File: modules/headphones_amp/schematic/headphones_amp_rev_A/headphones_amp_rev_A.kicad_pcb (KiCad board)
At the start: 2 copper layers, 24 parts, among them Q1 BC140, Q2 BC160, Q3 BC548, Q4 BC557, Q5 BC548, Q6 BC548

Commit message: added new references to the PPL
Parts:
- added C3: 220µ, Capacitor_THT:CP_Radial_D10.0mm_P5.00mm, F.Cu at (125.4, 64.0)
- added Q7: BC548, Package_TO_SOT_THT:TO-92L_Inline_Wide, F.Cu at (112.0, 111.4)
- added R13: 3.3k, Resistor_THT:R_Axial_DIN0207_L6.3mm_D2.5mm_P10.16mm_Horizontal, F.Cu at (110.2, 47.4)
- added R14: 1.5k, Resistor_THT:R_Axial_DIN0207_L6.3mm_D2.5mm_P10.16mm_Horizontal, F.Cu at (110.2, 51.5)
- added R15: 820, Resistor_THT:R_Axial_DIN0207_L6.3mm_D2.5mm_P10.16mm_Horizontal, F.Cu at (110.2, 55.5)
- added R16: 15k, Resistor_THT:R_Axial_DIN0207_L6.3mm_D2.5mm_P10.16mm_Horizontal, F.Cu at (110.2, 59.6)
- added R17: 56k, Resistor_THT:R_Axial_DIN0207_L6.3mm_D2.5mm_P10.16mm_Horizontal, F.Cu at (110.2, 63.6)
- added R18: 33k, Resistor_THT:R_Axial_DIN0207_L6.3mm_D2.5mm_P10.16mm_Horizontal, F.Cu at (110.2, 67.7)
- added R19: 10k, Resistor_THT:R_Axial_DIN0207_L6.3mm_D2.5mm_P10.16mm_Horizontal, F.Cu at (110.2, 71.7)
- added RV1: 820, Potentiometer_THT:Potentiometer_Bourns_3296W_Vertical, F.Cu at (130.0, 48.6)
- added RV2: 2.2k, Potentiometer_THT:Potentiometer_Bourns_3296W_Vertical, F.Cu at (130.0, 55.0)
- added TP1: TestPoint, TestPoint:TestPoint_Pad_D2.0mm, F.Cu at (135.0, 47.4)
- added TP2: TestPoint, TestPoint:TestPoint_Pad_D2.0mm, F.Cu at (135.0, 51.5)
- C1: value 100µ -> 220µ
- R5: value 1.2k -> 2.2k
- R8: value 330 -> 470
- moved R2 67.2 mm to (128.6, 117.5), turned to 180 degrees
- moved C1 59.7 mm to (137.0, 114.0)
- moved R1 56.6 mm to (118.4, 110.0)
- moved Q1 36.2 mm to (118.5, 104.5), turned to 90 degrees
- moved Q2 35.8 mm to (118.5, 124.5), turned to -90 degrees
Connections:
- C1 pad 2: unconnected-(C1-Pad2) -> Net-(C1-Pad2)
- Q1 pad 2: Net-(D1-A) -> Net-(Q1-B)
- Q2 pad 2: Net-(D3-K) -> Net-(Q2-B)
- Q5 pad 1: Net-(D3-K) -> Net-(Q2-B)
- Q5 pad 2: unconnected-(Q5-B-Pad2) -> Net-(Q5-B)
- R5 pad 2: Net-(D1-A) -> Net-(Q1-B)

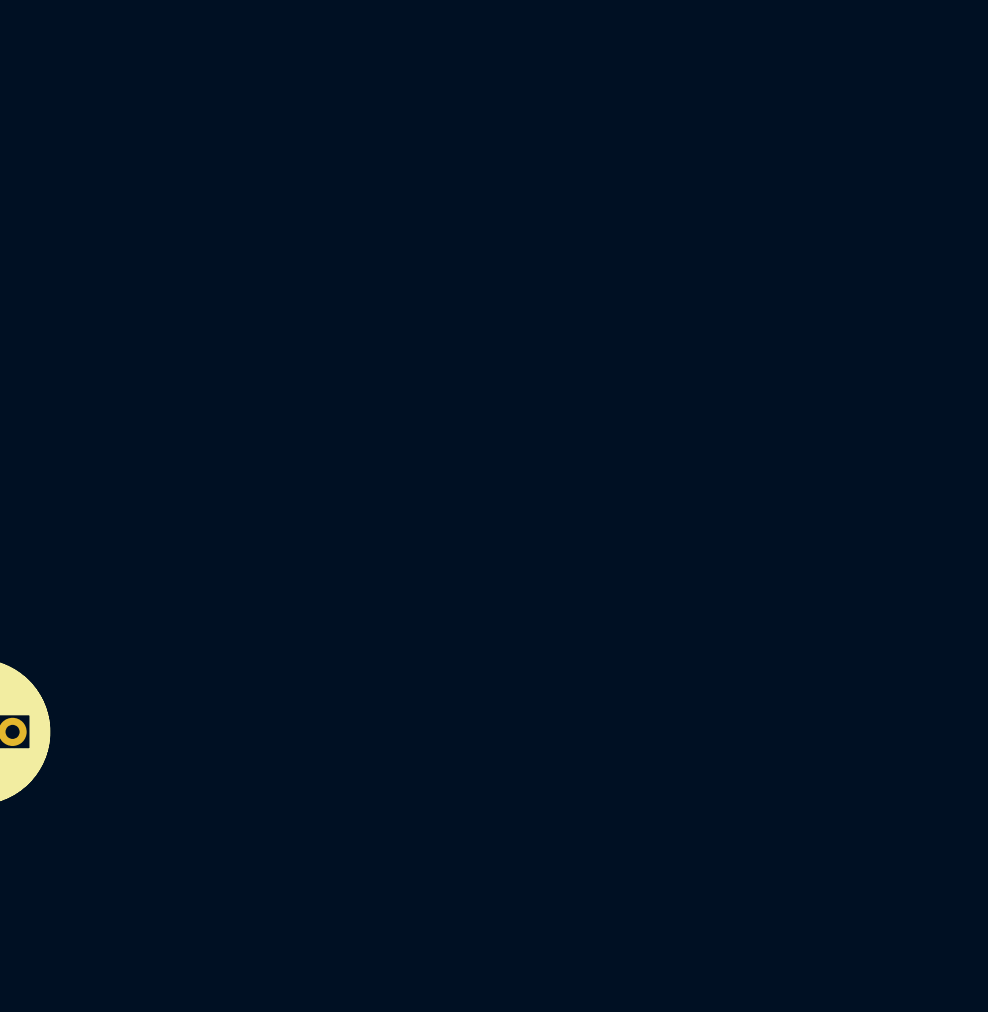
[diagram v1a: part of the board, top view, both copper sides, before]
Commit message: added proper silkscreen on PTV potentiometer
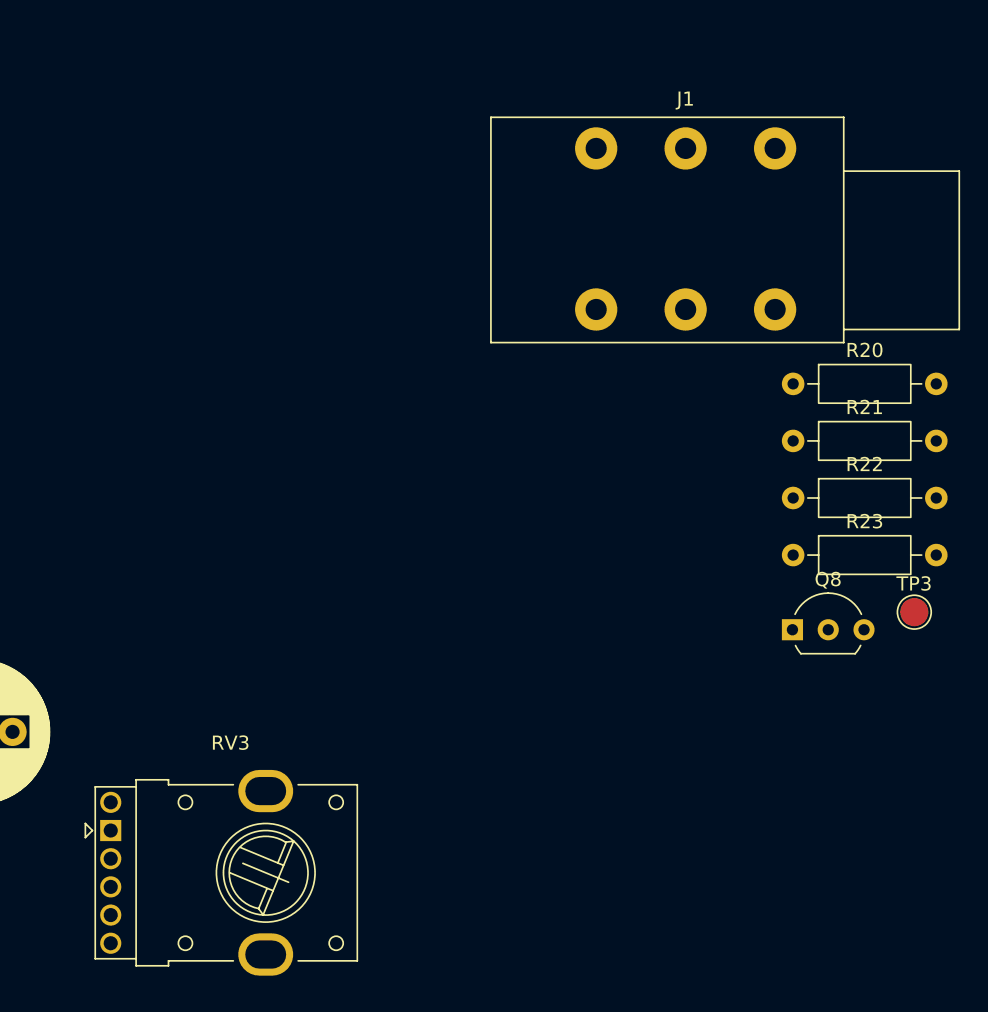
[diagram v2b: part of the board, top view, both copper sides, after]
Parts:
- added J1: AudioJack3_SwitchTR, Connector_Audio:Jack_6.35mm_Neutrik_NRJ6HM-1-PRE_Horizontal, F.Cu at (183.4, 72.6)
- added Q8: BC557, Package_TO_SOT_THT:TO-92L_Inline_Wide, F.Cu at (197.3, 106.8)
- added R20: 470, Resistor_THT:R_Axial_DIN0207_L6.3mm_D2.5mm_P10.16mm_Horizontal, F.Cu at (197.4, 89.3)
- added R21: 100, Resistor_THT:R_Axial_DIN0207_L6.3mm_D2.5mm_P10.16mm_Horizontal, F.Cu at (197.4, 93.3)
- added R22: 470, Resistor_THT:R_Axial_DIN0207_L6.3mm_D2.5mm_P10.16mm_Horizontal, F.Cu at (197.4, 97.4)
- added R23: 470, Resistor_THT:R_Axial_DIN0207_L6.3mm_D2.5mm_P10.16mm_Horizontal, F.Cu at (197.4, 101.5)
- added RV3: 68k, Potentiometer_THT:Potentiometer_Bourns_PTV112-4_Dual_Vertical, F.Cu at (149.0, 121.0)
- added TP3: TestPoint, TestPoint:TestPoint_Pad_D2.0mm, F.Cu at (206.0, 105.5)
- R15: value 820 -> 680
- R16: value 15k -> 10k
- R17: value 56k -> 3.3k
- R19: value 10k -> 68k
- RV1: value 820 -> 1k
- RV2: value 2.2k -> 4.7k
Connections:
- net Net-(C1-Pad2) renamed out_L
- C3 pad 1: unconnected-(C3-Pad1) -> Net-(Q8-C)

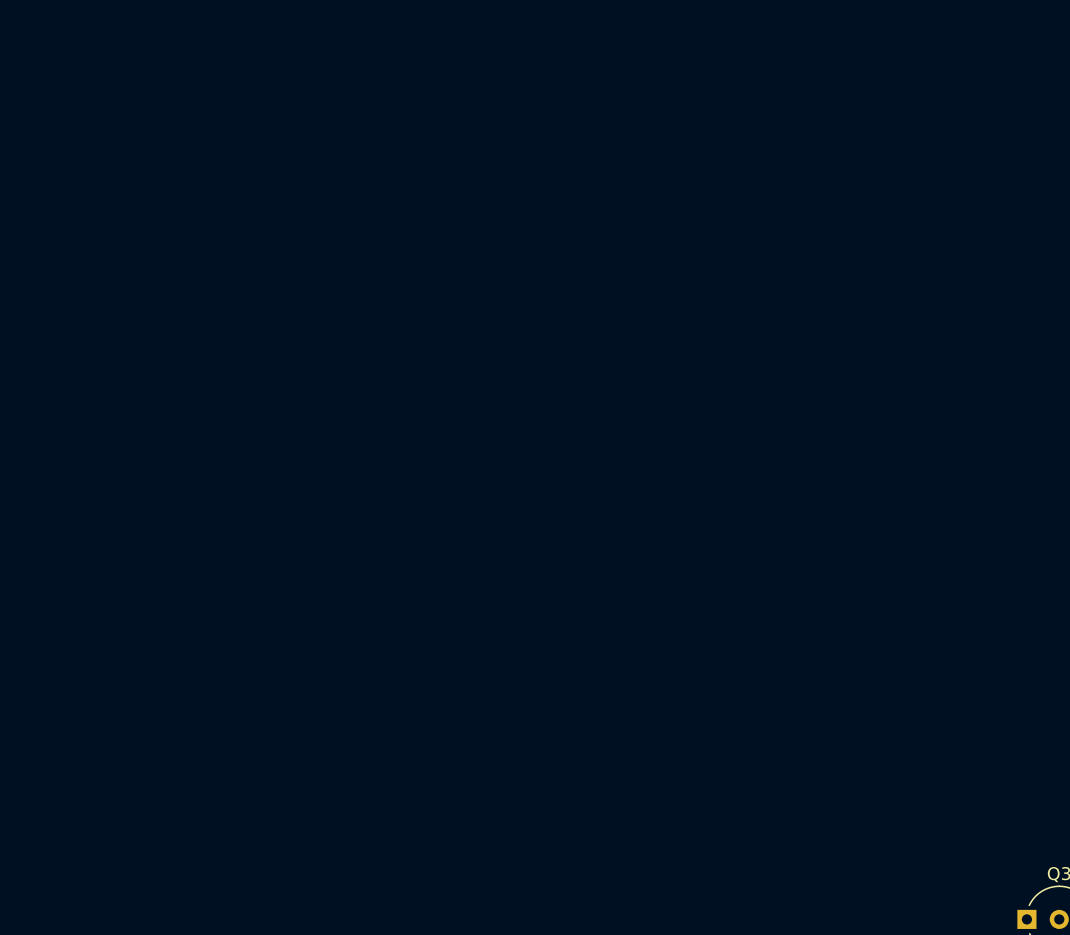
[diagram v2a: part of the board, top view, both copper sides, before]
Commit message: updated the Bourns PTV112 updated schematic renamed and upgraded the list of commonly used kicad parts
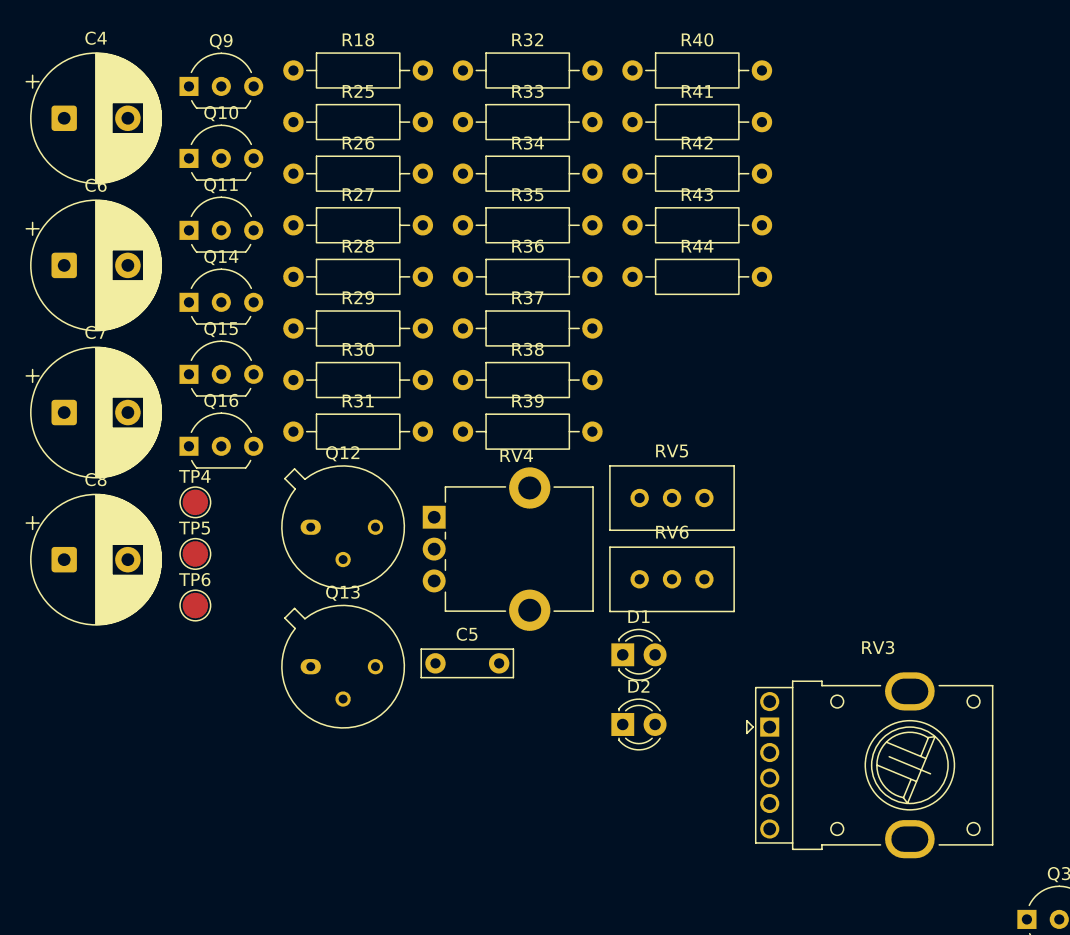
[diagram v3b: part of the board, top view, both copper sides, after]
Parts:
- added C4: 220µ, Capacitor_THT:CP_Radial_D10.0mm_P5.00mm, F.Cu at (17.6, 22.4)
- added C5: 100nF, Capacitor_THT:C_Rect_L7.0mm_W2.0mm_P5.00mm, F.Cu at (46.8, 65.2)
- added C6: 220µ, Capacitor_THT:CP_Radial_D10.0mm_P5.00mm, F.Cu at (17.6, 34.0)
- added C7: 220µ, Capacitor_THT:CP_Radial_D10.0mm_P5.00mm, F.Cu at (17.6, 45.5)
- added C8: 100µ, Capacitor_THT:CP_Radial_D10.0mm_P5.00mm, F.Cu at (17.6, 57.1)
- added D1: Green, LED_THT:LED_D3.0mm, F.Cu at (61.5, 64.5)
- added D2: Red, LED_THT:LED_D3.0mm, F.Cu at (61.5, 70.0)
- added Q10: BC548, Package_TO_SOT_THT:TO-92L_Inline_Wide, F.Cu at (27.4, 25.6)
- added Q11: BC548, Package_TO_SOT_THT:TO-92L_Inline_Wide, F.Cu at (27.4, 31.2)
- added Q12: BC140, Package_TO_SOT_THT:TO-39-3, F.Cu at (37.0, 54.5)
- added Q13: BC160, Package_TO_SOT_THT:TO-39-3, F.Cu at (37.0, 65.5)
- added Q14: BC548, Package_TO_SOT_THT:TO-92L_Inline_Wide, F.Cu at (27.4, 36.9)
- added Q15: BC557, Package_TO_SOT_THT:TO-92L_Inline_Wide, F.Cu at (27.4, 42.5)
- added Q16: BC548, Package_TO_SOT_THT:TO-92L_Inline_Wide, F.Cu at (27.4, 48.2)
- added Q9: BC557, Package_TO_SOT_THT:TO-92L_Inline_Wide, F.Cu at (27.4, 19.9)
- added R18: 470, Resistor_THT:R_Axial_DIN0207_L6.3mm_D2.5mm_P10.16mm_Horizontal, F.Cu at (35.6, 18.7)
- added R25: 2.2k, Resistor_THT:R_Axial_DIN0207_L6.3mm_D2.5mm_P10.16mm_Horizontal, F.Cu at (35.6, 22.7)
- added R26: 68k, Resistor_THT:R_Axial_DIN0207_L6.3mm_D2.5mm_P10.16mm_Horizontal, F.Cu at (35.6, 26.8)
- added R27: 3.3k, Resistor_THT:R_Axial_DIN0207_L6.3mm_D2.5mm_P10.16mm_Horizontal, F.Cu at (35.6, 30.8)
- added R28: 10k, Resistor_THT:R_Axial_DIN0207_L6.3mm_D2.5mm_P10.16mm_Horizontal, F.Cu at (35.6, 34.9)
- added R29: 1.5k, Resistor_THT:R_Axial_DIN0207_L6.3mm_D2.5mm_P10.16mm_Horizontal, F.Cu at (35.6, 38.9)
- added R30: 680, Resistor_THT:R_Axial_DIN0207_L6.3mm_D2.5mm_P10.16mm_Horizontal, F.Cu at (35.6, 43.0)
- added R31: 2.2k, Resistor_THT:R_Axial_DIN0207_L6.3mm_D2.5mm_P10.16mm_Horizontal, F.Cu at (35.6, 47.0)
- added R32: 470, Resistor_THT:R_Axial_DIN0207_L6.3mm_D2.5mm_P10.16mm_Horizontal, F.Cu at (48.9, 18.7)
- added R33: 10, Resistor_THT:R_Axial_DIN0207_L6.3mm_D2.5mm_P10.16mm_Horizontal, F.Cu at (48.9, 22.7)
- added R34: 4.7, Resistor_THT:R_Axial_DIN0207_L6.3mm_D2.5mm_P10.16mm_Horizontal, F.Cu at (48.9, 26.8)
- added R35: 4.7, Resistor_THT:R_Axial_DIN0207_L6.3mm_D2.5mm_P10.16mm_Horizontal, F.Cu at (48.9, 30.8)
- added R36: 22, Resistor_THT:R_Axial_DIN0207_L6.3mm_D2.5mm_P10.16mm_Horizontal, F.Cu at (48.9, 34.9)
- added R37: 1k, Resistor_THT:R_Axial_DIN0207_L6.3mm_D2.5mm_P10.16mm_Horizontal, F.Cu at (48.9, 38.9)
- added R38: 1k, Resistor_THT:R_Axial_DIN0207_L6.3mm_D2.5mm_P10.16mm_Horizontal, F.Cu at (48.9, 43.0)
- added R39: 1k, Resistor_THT:R_Axial_DIN0207_L6.3mm_D2.5mm_P10.16mm_Horizontal, F.Cu at (48.9, 47.0)
- added R40: 1k, Resistor_THT:R_Axial_DIN0207_L6.3mm_D2.5mm_P10.16mm_Horizontal, F.Cu at (62.2, 18.7)
- added R41: 1k, Resistor_THT:R_Axial_DIN0207_L6.3mm_D2.5mm_P10.16mm_Horizontal, F.Cu at (62.2, 22.7)
- added R42: 1k, Resistor_THT:R_Axial_DIN0207_L6.3mm_D2.5mm_P10.16mm_Horizontal, F.Cu at (62.2, 26.8)
- added R43: 3.3k, Resistor_THT:R_Axial_DIN0207_L6.3mm_D2.5mm_P10.16mm_Horizontal, F.Cu at (62.2, 30.8)
- added R44: 100, Resistor_THT:R_Axial_DIN0207_L6.3mm_D2.5mm_P10.16mm_Horizontal, F.Cu at (62.2, 34.9)
- added RV3: 68k, ProjectLib_Transient:Potentiometer_Bourns_PTV112-4_Dual_Vertical, F.Cu at (73.0, 70.2)
- added RV4: 1k, Potentiometer_THT:Potentiometer_Alpha_RD901F-40-00D_Single_Vertical_CircularHoles, F.Cu at (46.7, 53.7)
- added RV5: 4.7k, Potentiometer_THT:Potentiometer_Bourns_3296W_Vertical, F.Cu at (67.9, 52.2)
- added RV6: 1k, Potentiometer_THT:Potentiometer_Bourns_3296W_Vertical, F.Cu at (67.9, 58.6)
- added TP4: TestPoint, TestPoint:TestPoint_Pad_D2.0mm, F.Cu at (27.9, 52.6)
- added TP5: TestPoint, TestPoint:TestPoint_Pad_D2.0mm, F.Cu at (27.9, 56.6)
- added TP6: TestPoint, TestPoint:TestPoint_Pad_D2.0mm, F.Cu at (27.9, 60.7)
- D4: value LED -> Red
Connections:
- J1 pad R: unconnected-(J1-PadR) -> out_R
- R21 pad 2: unconnected-(R21-Pad2) -> Net-(R21-Pad2)

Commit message: added footprint for the ANT switch
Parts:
- added H1: MountingHole_Pad, MountingHole:MountingHole_3.2mm_M3_Pad_Via, F.Cu at (153.8, 56.5)
- added H2: MountingHole_Pad, MountingHole:MountingHole_3.2mm_M3_Pad_Via, F.Cu at (153.8, 64.4)
- added H3: MountingHole_Pad, MountingHole:MountingHole_3.2mm_M3_Pad_Via, F.Cu at (153.8, 72.4)
- added H4: MountingHole_Pad, MountingHole:MountingHole_3.2mm_M3_Pad_Via, F.Cu at (153.8, 80.3)
- added J2: AudioJack3_SwitchTR, Connector_Audio:Jack_3.5mm_CUI_SJ1-3515N_Horizontal, F.Cu at (237.4, 53.3)
- added SW1: SW_SPDT, Button_Switch_SMD:SW_SPST_Omron_B3FS-100xP, F.Cu at (163.4, 56.4)
- C4: value 220µ -> 47µF

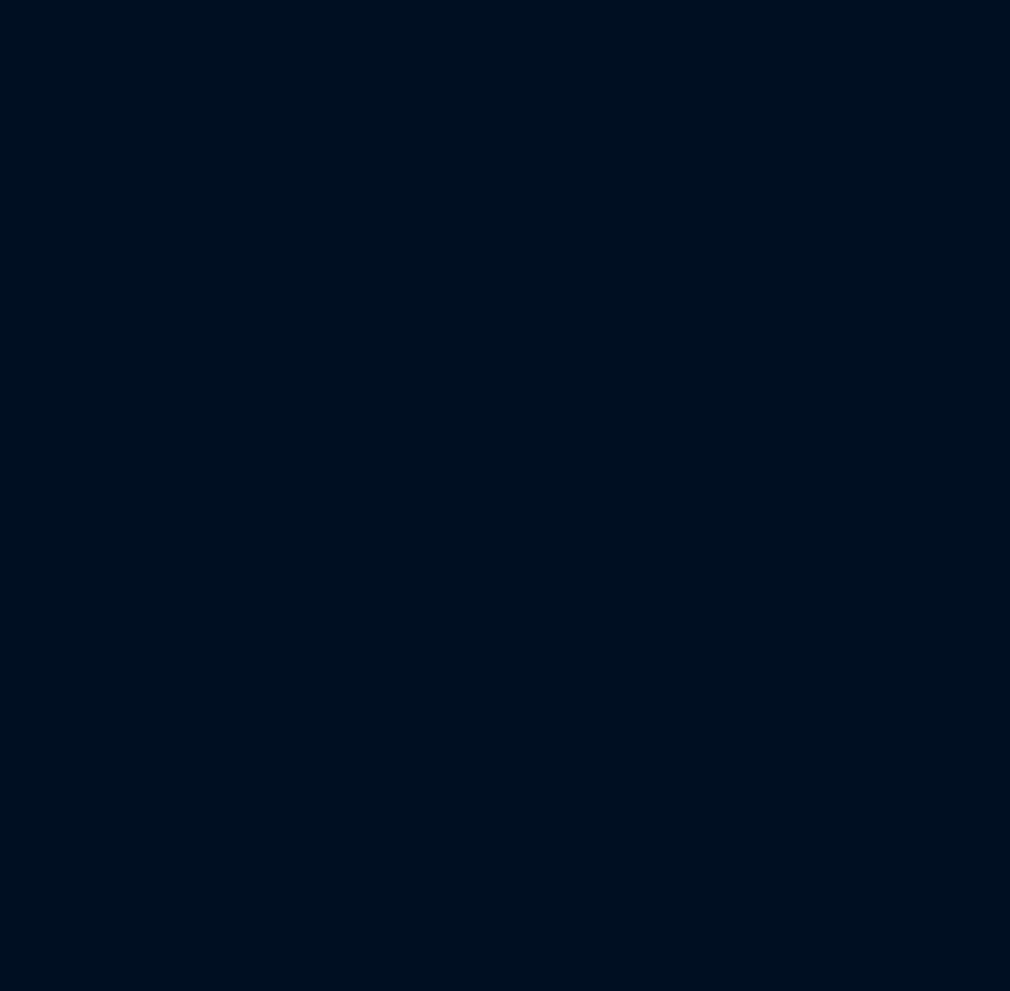
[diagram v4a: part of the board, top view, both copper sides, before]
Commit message: updated ignore list updated library with a new switch (ANT)
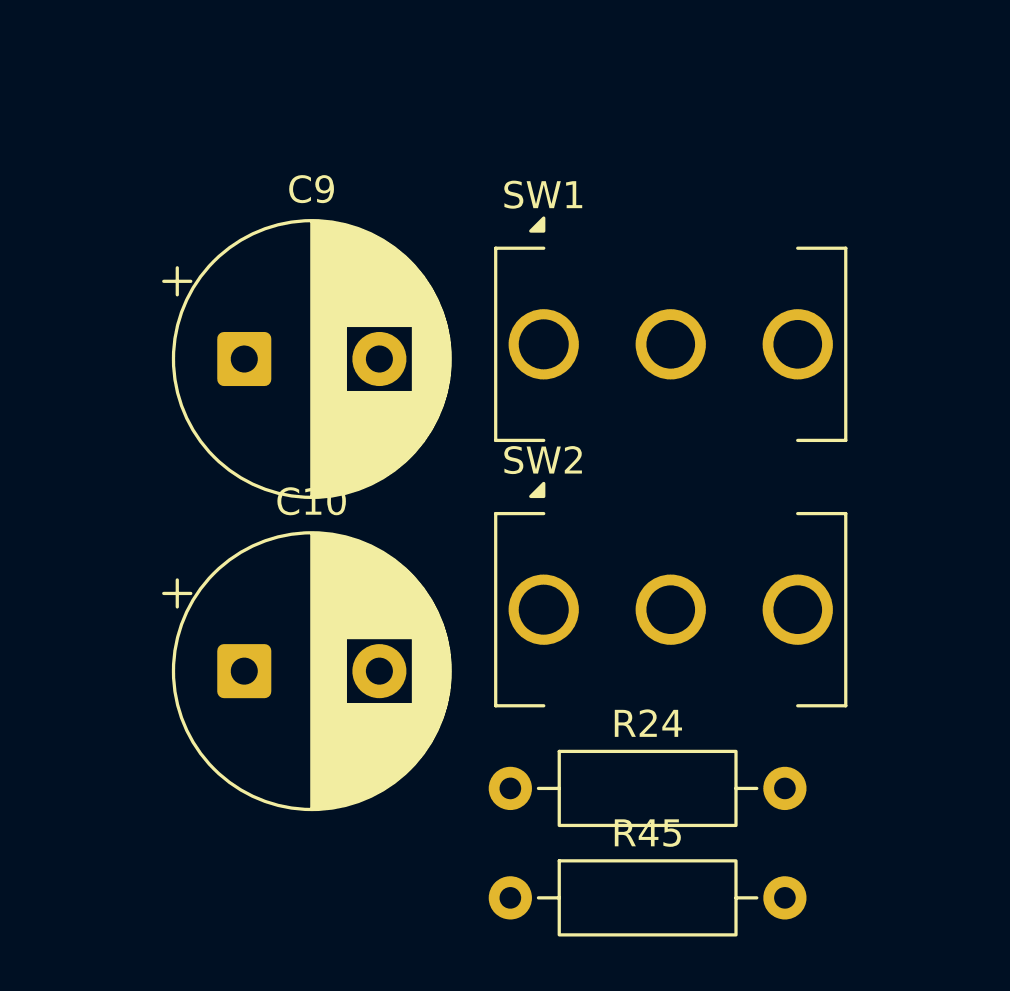
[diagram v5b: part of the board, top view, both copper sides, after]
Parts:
- added C10: 220µ, Capacitor_THT:CP_Radial_D10.0mm_P5.00mm, F.Cu at (181.0, 135.1)
- added C9: 220µ, Capacitor_THT:CP_Radial_D10.0mm_P5.00mm, F.Cu at (181.0, 123.6)
- added R24: 470, Resistor_THT:R_Axial_DIN0207_L6.3mm_D2.5mm_P10.16mm_Horizontal, F.Cu at (190.8, 139.4)
- added R45: 470, Resistor_THT:R_Axial_DIN0207_L6.3mm_D2.5mm_P10.16mm_Horizontal, F.Cu at (190.8, 143.5)
- added SW1: SW_SPDT, ProjectLib_Transient:SW_CIT_ANT13_SPDT_Straight, F.Cu at (192.1, 123.0)
- added SW2: SW_SPDT, ProjectLib_Transient:SW_CIT_ANT13_SPDT_Straight, F.Cu at (192.1, 132.8)
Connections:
- RV3 pad 2: unconnected-(RV3-Pad2) -> Net-(C9-Pad1)
- RV3 pad 5: unconnected-(RV3B-2-Pad5) -> Net-(RV3B-2)
